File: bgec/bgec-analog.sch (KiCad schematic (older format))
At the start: 7 parts

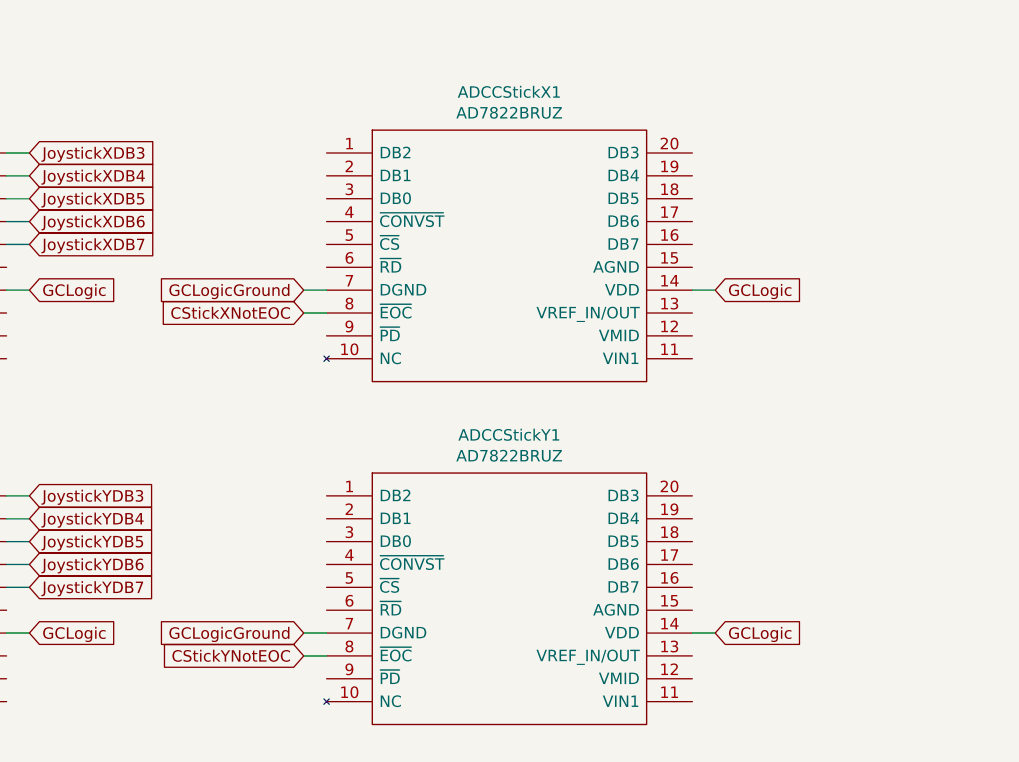
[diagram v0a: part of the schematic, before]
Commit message: Add more ADC connections
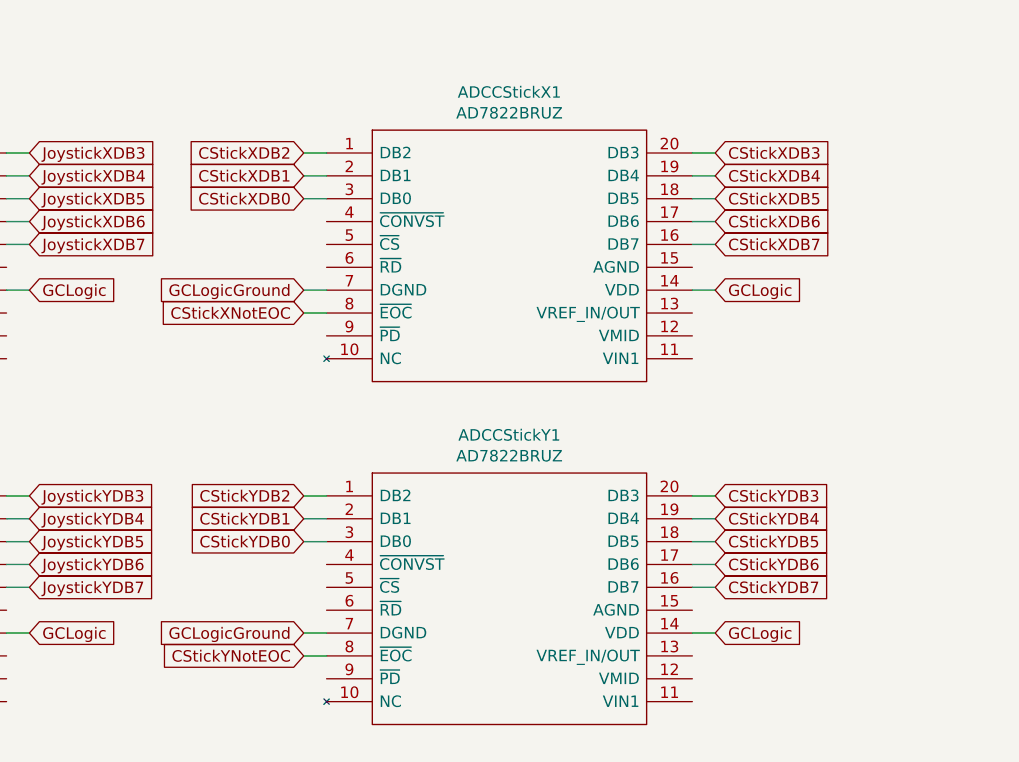
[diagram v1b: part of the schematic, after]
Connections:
- net labels added: CStickXDB0, CStickXDB1, CStickXDB2, CStickXDB3, CStickXDB4, CStickXDB5, CStickXDB6, CStickXDB7, CStickYDB0, CStickYDB1, CStickYDB2, CStickYDB3, CStickYDB4, CStickYDB5, CStickYDB6, CStickYDB7
- wire segments 66 -> 82
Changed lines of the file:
@@
 Wire Wire Line
 	10250 700  10250 750
+Text GLabel 4400 2700 0    50   Input ~ 0
+CStickYDB0
+Text GLabel 4400 2600 0    50   Input ~ 0
+CStickYDB1
+Text GLabel 4400 2500 0    50   Input ~ 0
+CStickYDB2
+Text GLabel 6200 2500 2    50   Input ~ 0
+CStickYDB3
+Text GLabel 6200 2600 2    50   Input ~ 0
+CStickYDB4
+Text GLabel 6200 2700 2    50   Input ~ 0
+CStickYDB5
+Text GLabel 6200 2800 2    50   Input ~ 0
+CStickYDB6
+Text GLabel 6200 2900 2    50   Input ~ 0
+CStickYDB7
+Wire Wire Line
+	4400 2500 4500 2500
+Wire Wire Line
+	4500 2600 4400 2600
+Wire Wire Line
+	4400 2700 4500 2700
+Wire Wire Line
+	6100 2900 6200 2900
+Wire Wire Line
+	6200 2800 6100 2800
+Wire Wire Line
+	6100 2700 6200 2700
+Wire Wire Line
+	6200 2600 6100 2600
+Wire Wire Line
+	6100 2500 6200 2500
+Text GLabel 4400 1200 0    50   Input ~ 0
+CStickXDB0
+Text GLabel 4400 1100 0    50   Input ~ 0
+CStickXDB1
+Text GLabel 4400 1000 0    50   Input ~ 0
+CStickXDB2
+Wire Wire Line
+	4400 1000 4500 1000
+Wire Wire Line
+	4500 1100 4400 1100
+Wire Wire Line
+	4400 1200 4500 1200
+Text GLabel 6200 1000 2    50   Input ~ 0
+CStickXDB3
+Text GLabel 6200 1100 2    50   Input ~ 0
+CStickXDB4
+Text GLabel 6200 1200 2    50   Input ~ 0
+CStickXDB5
+Text GLabel 6200 1300 2    50   Input ~ 0
+CStickXDB6
+Text GLabel 6200 1400 2    50   Input ~ 0
+CStickXDB7
+Wire Wire Line
+	6100 1400 6200 1400
+Wire Wire Line
+	6200 1300 6100 1300
+Wire Wire Line
+	6100 1200 6200 1200
+Wire Wire Line
+	6200 1100 6100 1100
+Wire Wire Line
+	6100 1000 6200 1000
 $EndSCHEMATC

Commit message: Properly feed all ADC pins to the FPGA
Includes rudimentary routing. In the future I'm definitely going to move the ADCs closer to their joysticks/triggers so the model doesn't look like a swastika.
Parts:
- removed ADCStateInverter1: 74HC04, LibraryLoader:SON65P440X500X110-14N, symbol 74xx:74HC04
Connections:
- net labels added: CStickXNotCONVST, CStickXNotCS, CStickXNotRD, CStickYNotCONVST, CStickYNotCS, CStickYNotRD, JoystickXNotCONVST, JoystickXNotCS, JoystickXNotRD, JoystickYNotCONVST, JoystickYNotCS, JoystickYNotRD, TriggerLNotCONVST, TriggerLNotCS, TriggerLNotRD, TriggerRNotCONVST, TriggerRNotCS, TriggerRNotRD
- net labels removed: CStickXEOC, CStickYEOC, JoystickXEOC, JoystickYEOC, TriggerLEOC, TriggerREOC
- wire segments 82 -> 90
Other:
- moved on the sheet: ADCCStickX1, ADCCStickY1, ADCTriggerR1
